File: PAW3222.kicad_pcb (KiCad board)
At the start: 2 copper layers, 7.8 x 12.5 mm, 7 parts, among them J1 Conn_01x06_Socket, U1 PAW3220LU

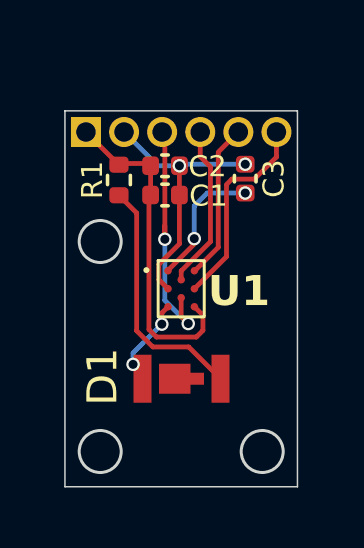
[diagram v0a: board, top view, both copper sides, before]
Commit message: update pcb to ffc cable connector
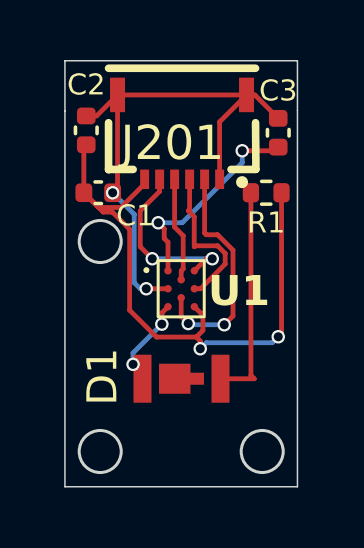
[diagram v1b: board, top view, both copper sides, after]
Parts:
- removed J1: Conn_01x06_Socket, Connector_PinHeader_1.27mm:PinHeader_1x06_P1.27mm_Vertical
- added J201: Conn_01x06_MountingPin, paw3222:GT-F0501SR10-06S1101, F.Cu at (143.0, 77.7)
- moved R1 4.93 mm to (145.8, 79.6), turned to 0 degrees
- moved C2 2.88 mm to (139.8, 77.5), turned to 90 degrees
- moved C1 2.23 mm to (140.2, 79.6)
- moved C3 1.88 mm to (146.2, 77.6)
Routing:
- net VCC 3.3V: track 10.8 -> 20.7 mm, vias 0 -> 2
- net GND: track 9.03 -> 18.0 mm
- net Net-(U1-VDDA): track 4.91 -> 7.07 mm
- net MOTION: track 5.44 -> 3.49 mm
- net SDIO: track 7.08 -> 5.22 mm
- net Net-(D1-A): track 8.22 -> 7.37 mm
- net SCLK: track 8.39 -> 7.77 mm
- net NCS: track 5.52 -> 5.86 mm, vias 0 -> 2
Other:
- board size 7.8 x 12.5 mm -> 7.8 x 14.2 mm
- board text added: "SCLK"
- board text added: "SDIO"
- board text added: "modified Jonavano"
- board text removed: "DIO"
- board text removed: "SCK"

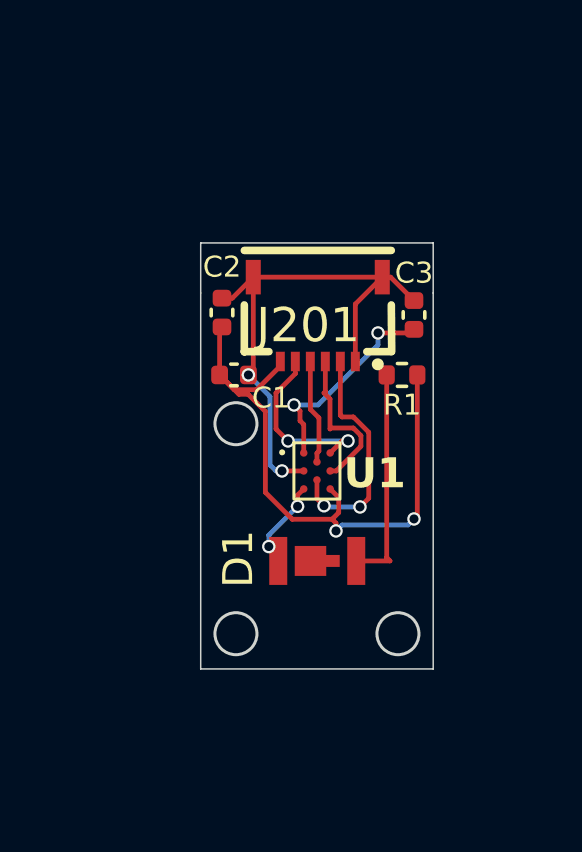
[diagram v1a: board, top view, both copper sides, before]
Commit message: flip pin out
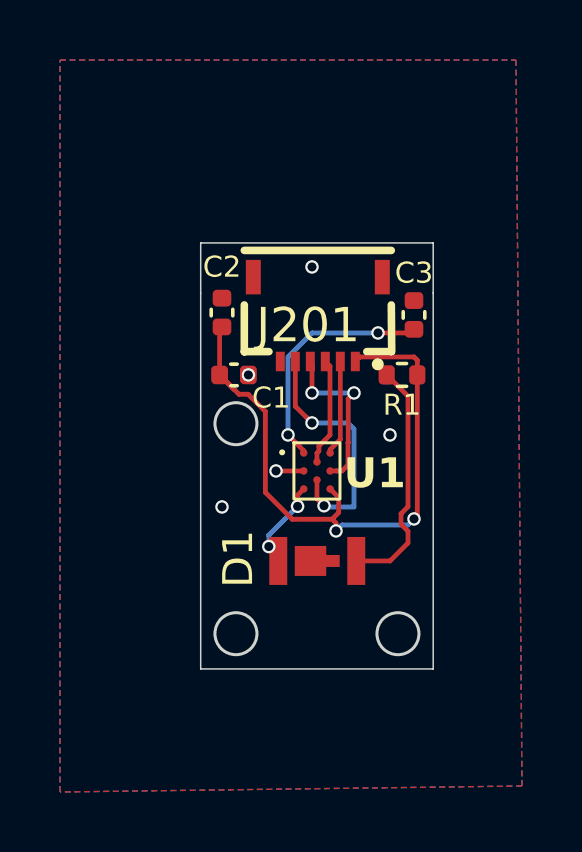
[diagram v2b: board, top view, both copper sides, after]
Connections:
- J201 pad 1: GND -> VCC 3.3V
- J201 pad 2: SCLK -> NCS
- J201 pad 3: SDIO -> MOTION
- J201 pad 4: MOTION -> SDIO
- J201 pad 5: NCS -> SCLK
- J201 pad 6: VCC 3.3V -> GND
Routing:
- net GND: track 18.0 -> 1.51 mm, vias 2 -> 5
- net NCS: track 5.86 -> 3.20 mm, vias 2 -> 0
- net Net-(U1-VDDA): track 7.07 -> 8.00 mm
- net SCLK: track 7.77 -> 8.63 mm
- net Net-(D1-A): track 7.37 -> 8.06 mm
- net VCC 3.3V: track 20.7 -> 21.4 mm
- net SDIO: track 5.22 -> 5.63 mm, vias 0 -> 2
- added copper zone on B.Cu, net GND
- added copper zone on F.Cu, net GND
